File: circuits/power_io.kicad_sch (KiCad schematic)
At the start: 53 parts, among them J5 24V DC IN, J6 24V RJ45 IN, U11 AP2112K-3.3, U12 INA4180A1, U13 LM4040C50 5V, U14 AD7606BSTZ-4, U15 AP63205WU-7 5V BUCK, U16 AP63200WU-7 10.7V BUCK

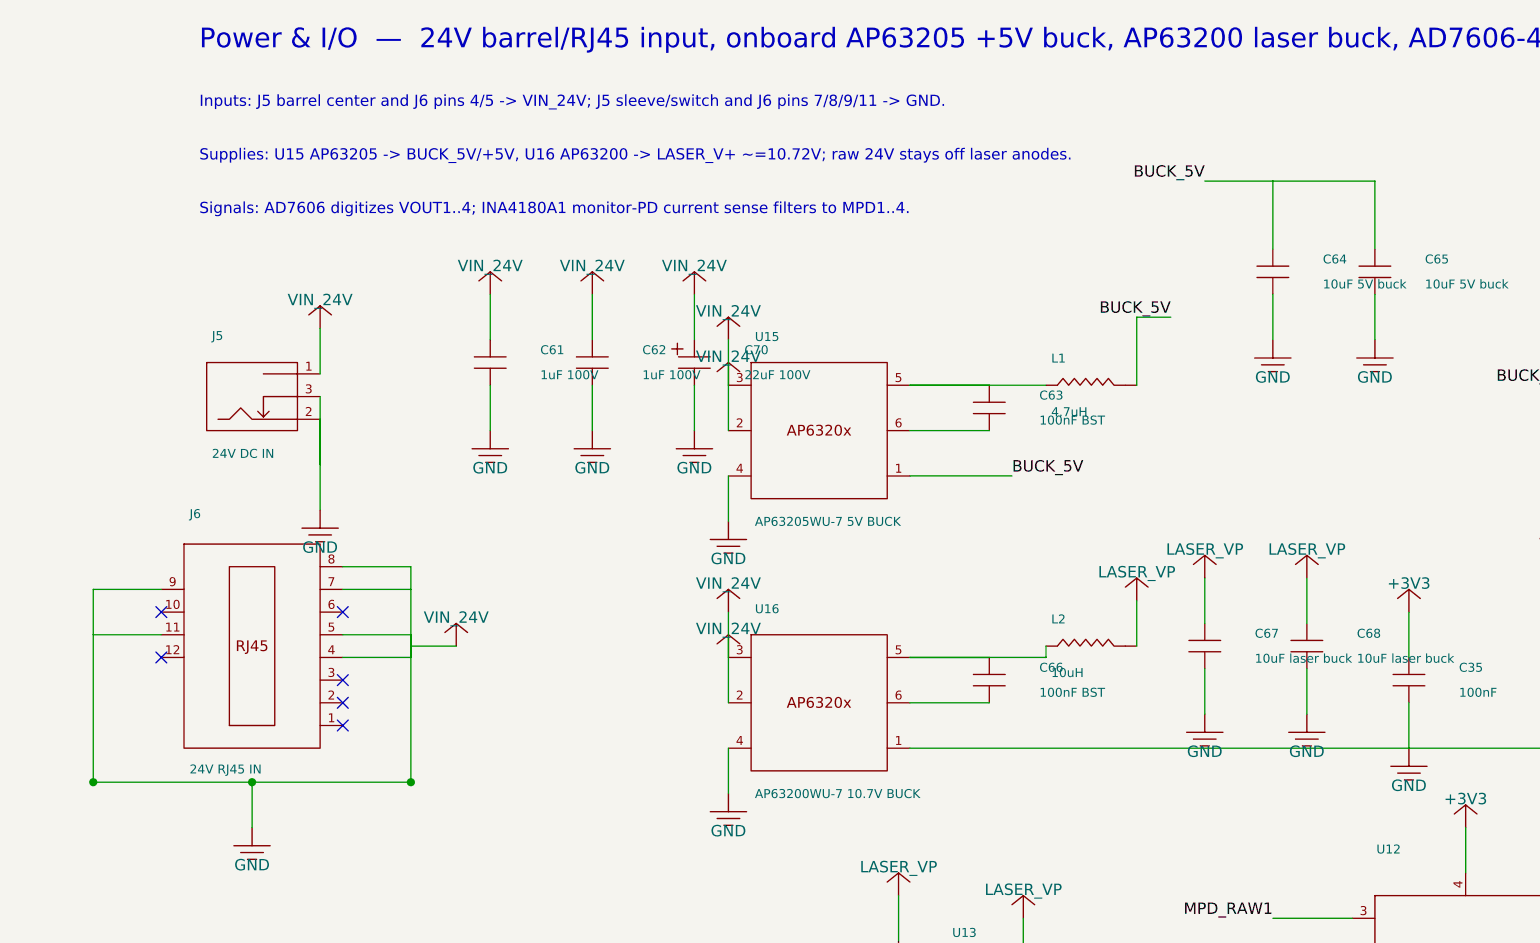
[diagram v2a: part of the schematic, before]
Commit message: Use access-controller RJ45 in power IO
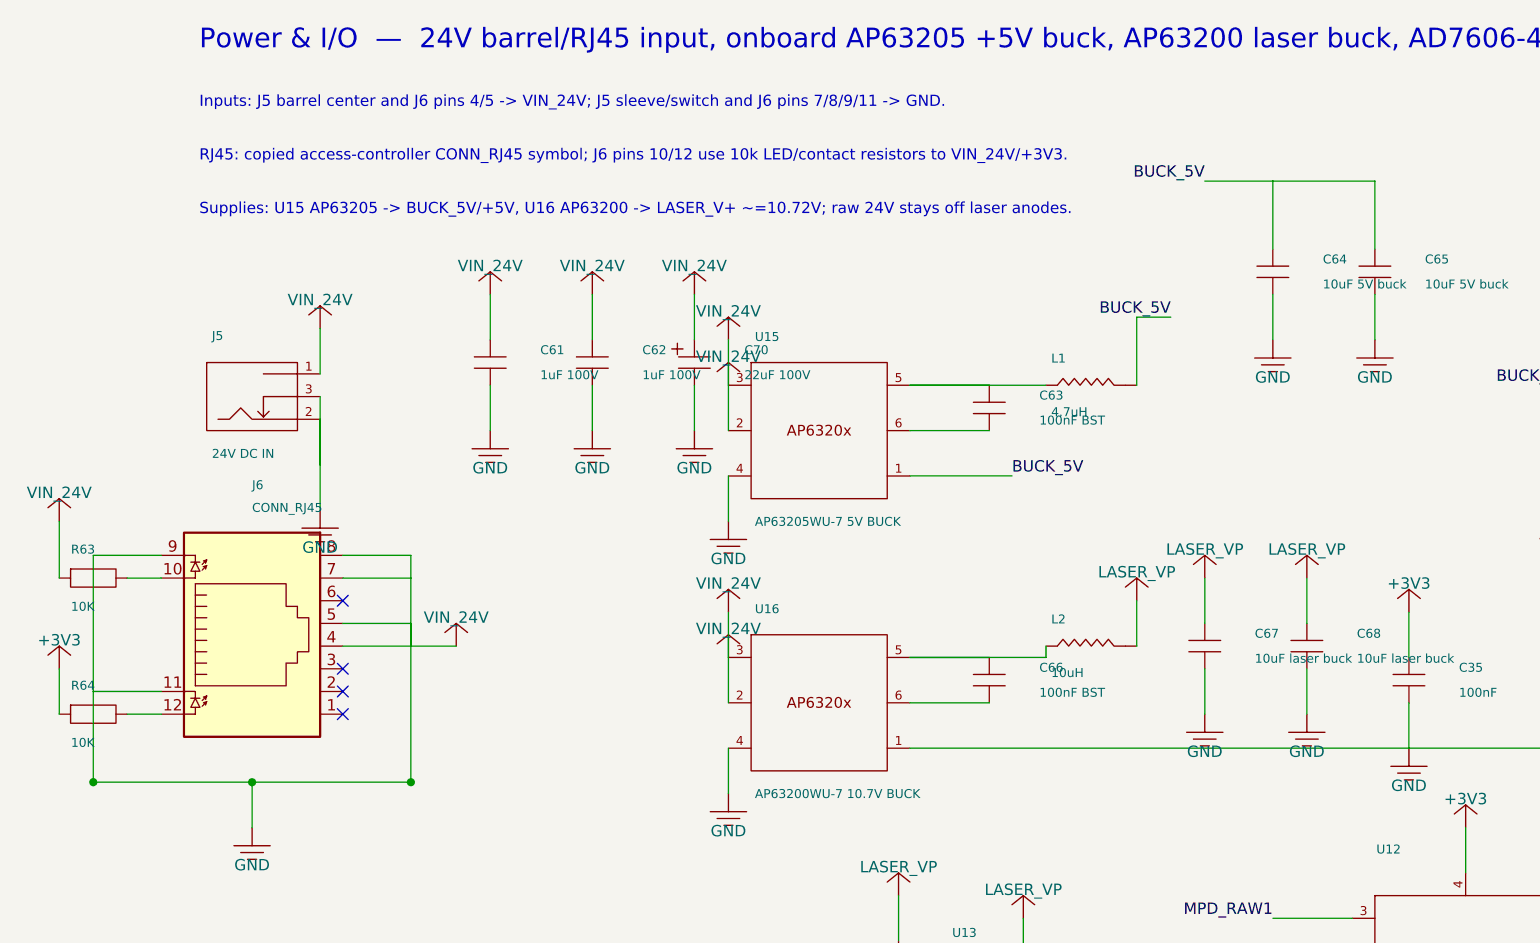
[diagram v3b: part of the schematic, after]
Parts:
- removed C35, C49: 100nF, Capacitor_SMD:C_0402_1005Metric_Pad0.74x0.62mm_HandSolder, symbol viv:C_V
- removed C36: 100nF MPD bias, Capacitor_SMD:C_0402_1005Metric_Pad0.74x0.62mm_HandSolder, symbol viv:C_V
- removed C51, C52: 100nF ADC AVCC, Capacitor_SMD:C_0402_1005Metric_Pad0.74x0.62mm_HandSolder, symbol viv:C_V
- removed C63, C66: 100nF BST, Capacitor_SMD:C_0402_1005Metric_Pad0.74x0.62mm_HandSolder, symbol viv:C_V
- removed L1: 4.7uH, Open_Automation:L_5.4x5.3_H3, symbol viv:L_H
- removed L2: 10uH, Open_Automation:L_4x4, symbol viv:L_H
- added C34: 10uF +5V bulk, Capacitor_SMD:C_0805_2012Metric_Pad1.18x1.45mm_HandSolder, symbol viv:C_V
- added C40: 100nF MPD ADC, Capacitor_SMD:C_0402_1005Metric_Pad0.74x0.62mm_HandSolder, symbol viv:C_V
- added C50: 10uF, Capacitor_SMD:C_0805_2012Metric_Pad1.18x1.45mm_HandSolder, symbol viv:C_V
- added C60: 10uF ADC REFCAP, Capacitor_SMD:C_0805_2012Metric_Pad1.18x1.45mm_HandSolder, symbol viv:C_V
- added C69: 100pF FF, Capacitor_SMD:C_0402_1005Metric_Pad0.74x0.62mm_HandSolder, symbol viv:C_V
- added C70: 22uF 100V, Capacitor_SMD:C_Elec_8x10.2, symbol viv:C_POL_V
- added R49: 1k ADC, Resistor_SMD:R_0603_1608Metric_Pad0.98x0.95mm_HandSolder, symbol viv:R_H
- added U12: INA4180A1, Package_SO:TSSOP-14_4.4x5mm_P0.65mm, symbol viv:INA4180_TSSOP14
- added U14: AD7606BSTZ-4, Package_QFP:LQFP-64_10x10mm_P0.5mm, symbol viv:AD7606_4
- added U15: AP63205WU-7 5V BUCK, Package_TO_SOT_SMD:TSOT-23-6, symbol viv:AP6320X_TSOT6
- added U16: AP63200WU-7 10.7V BUCK, Package_TO_SOT_SMD:TSOT-23-6, symbol viv:AP6320X_TSOT6
- C35: renamed from R41; value 2.49k MPD bias -> 100nF; footprint Resistor_SMD:R_0603_1608Metric_Pad0.98x0.95mm_HandSolder -> Capacitor_SMD:C_0402_1005Metric_Pad0.74x0.62mm_HandSolder; symbol viv:R_V -> viv:C_V; LCSC C2099849 -> C83056; Part Number CRCW06032K49FKEAHP -> 0402B104K160CT
- C36: renamed from R42; value 750R MPD sense -> 100nF MPD bias; footprint Resistor_SMD:R_0603_1608Metric_Pad0.98x0.95mm_HandSolder -> Capacitor_SMD:C_0402_1005Metric_Pad0.74x0.62mm_HandSolder; symbol viv:R_H -> viv:C_V; LCSC C114635 -> C83056; Part Number RC0603FR-07750RL -> 0402B104K160CT
- C37: renamed from R45; value 1k ADC -> 100nF MPD ADC; footprint Resistor_SMD:R_0603_1608Metric_Pad0.98x0.95mm_HandSolder -> Capacitor_SMD:C_0402_1005Metric_Pad0.74x0.62mm_HandSolder; symbol viv:R_H -> viv:C_V; LCSC C2907002 -> C83056; Part Number FRC0603F1001TS -> 0402B104K160CT
- C38: renamed from R47; value 1k ADC -> 100nF MPD ADC; footprint Resistor_SMD:R_0603_1608Metric_Pad0.98x0.95mm_HandSolder -> Capacitor_SMD:C_0402_1005Metric_Pad0.74x0.62mm_HandSolder; symbol viv:R_H -> viv:C_V; LCSC C2907002 -> C83056; Part Number FRC0603F1001TS -> 0402B104K160CT
- C39: renamed from R49; value 1k ADC -> 100nF MPD ADC; footprint Resistor_SMD:R_0603_1608Metric_Pad0.98x0.95mm_HandSolder -> Capacitor_SMD:C_0402_1005Metric_Pad0.74x0.62mm_HandSolder; symbol viv:R_H -> viv:C_V; LCSC C2907002 -> C83056; Part Number FRC0603F1001TS -> 0402B104K160CT
- C48: renamed from C50; value 10uF -> 1uF; footprint Capacitor_SMD:C_0805_2012Metric_Pad1.18x1.45mm_HandSolder -> Capacitor_SMD:C_0402_1005Metric_Pad0.74x0.62mm_HandSolder; LCSC C318691 -> C7472946; Part Number CL21A106KAYNNNG -> HGC0402R5105K250NTEJ
- C49: renamed from U16; value AP63200WU-7 10.7V BUCK -> 100nF; footprint Package_TO_SOT_SMD:TSOT-23-6 -> Capacitor_SMD:C_0402_1005Metric_Pad0.74x0.62mm_HandSolder; symbol viv:AP6320X_TSOT6 -> viv:C_V; LCSC C2071868 -> C83056; Part Number AP63200WU-7 -> 0402B104K160CT
- C53: renamed from C55; value 100nF ADC VDRIVE -> 100nF ADC AVCC
- C54: renamed from C56; value 10uF ADC AVCC -> 100nF ADC AVCC; footprint Capacitor_SMD:C_0805_2012Metric_Pad1.18x1.45mm_HandSolder -> Capacitor_SMD:C_0402_1005Metric_Pad0.74x0.62mm_HandSolder; LCSC C318691 -> C83056; Part Number CL21A106KAYNNNG -> 0402B104K160CT
- C55: renamed from C57; value 1uF ADC REGCAP -> 100nF ADC VDRIVE; LCSC C7472946 -> C83056; Part Number HGC0402R5105K250NTEJ -> 0402B104K160CT
- C56: renamed from C58; value 1uF ADC REGCAP -> 10uF ADC AVCC; footprint Capacitor_SMD:C_0402_1005Metric_Pad0.74x0.62mm_HandSolder -> Capacitor_SMD:C_0805_2012Metric_Pad1.18x1.45mm_HandSolder; LCSC C7472946 -> C318691; Part Number HGC0402R5105K250NTEJ -> CL21A106KAYNNNG
- C57: renamed from C59; value 10uF ADC REF -> 1uF ADC REGCAP; footprint Capacitor_SMD:C_0805_2012Metric_Pad1.18x1.45mm_HandSolder -> Capacitor_SMD:C_0402_1005Metric_Pad0.74x0.62mm_HandSolder; LCSC C318691 -> C7472946; Part Number CL21A106KAYNNNG -> HGC0402R5105K250NTEJ
- C58: renamed from C60; value 10uF ADC REFCAP -> 1uF ADC REGCAP; footprint Capacitor_SMD:C_0805_2012Metric_Pad1.18x1.45mm_HandSolder -> Capacitor_SMD:C_0402_1005Metric_Pad0.74x0.62mm_HandSolder; LCSC C318691 -> C7472946; Part Number CL21A106KAYNNNG -> HGC0402R5105K250NTEJ
- C59: renamed from U12; value INA4180A1 -> 10uF ADC REF; footprint Package_SO:TSSOP-14_4.4x5mm_P0.65mm -> Capacitor_SMD:C_0805_2012Metric_Pad1.18x1.45mm_HandSolder; symbol viv:INA4180_TSSOP14 -> viv:C_V; LCSC C2057528 -> C318691; Part Number INA4180A1IPWR -> CL21A106KAYNNNG
- C61: renamed from C70; value 22uF 100V -> 1uF 100V; footprint Capacitor_SMD:C_Elec_8x10.2 -> Capacitor_SMD:C_1206_3216Metric_Pad1.33x1.80mm_HandSolder; symbol viv:C_POL_V -> viv:C_V; LCSC C90264 -> C13832; Part Number RVT2A220M0810 -> CL31B105KCHNNNE
- C62: renamed from U15; value AP63205WU-7 5V BUCK -> 1uF 100V; footprint Package_TO_SOT_SMD:TSOT-23-6 -> Capacitor_SMD:C_1206_3216Metric_Pad1.33x1.80mm_HandSolder; symbol viv:AP6320X_TSOT6 -> viv:C_V; LCSC C2071056 -> C13832; Part Number AP63205WU-7 -> CL31B105KCHNNNE
- C63: renamed from C65; value 10uF 5V buck -> 100nF BST; footprint Capacitor_SMD:C_0805_2012Metric_Pad1.18x1.45mm_HandSolder -> Capacitor_SMD:C_0402_1005Metric_Pad0.74x0.62mm_HandSolder; LCSC C318691 -> C83056; Part Number CL21A106KAYNNNG -> 0402B104K160CT
- C64: renamed from D5; value SS14 -> 10uF 5V buck; footprint Diode_SMD:D_SMA -> Capacitor_SMD:C_0805_2012Metric_Pad1.18x1.45mm_HandSolder; symbol viv:SCHOTTKY -> viv:C_V; LCSC C2480 -> C318691; Part Number SS14 -> CL21A106KAYNNNG
- C65: renamed from D6; value SS14 -> 10uF 5V buck; footprint Diode_SMD:D_SMA -> Capacitor_SMD:C_0805_2012Metric_Pad1.18x1.45mm_HandSolder; symbol viv:SCHOTTKY -> viv:C_V; LCSC C2480 -> C318691; Part Number SS14 -> CL21A106KAYNNNG
- C66: renamed from C68; value 10uF laser buck -> 100nF BST; footprint Capacitor_SMD:C_0805_2012Metric_Pad1.18x1.45mm_HandSolder -> Capacitor_SMD:C_0402_1005Metric_Pad0.74x0.62mm_HandSolder; LCSC C318691 -> C83056; Part Number CL21A106KAYNNNG -> 0402B104K160CT
- C67: renamed from R61; value 274k FB -> 10uF laser buck; footprint Resistor_SMD:R_0603_1608Metric_Pad0.98x0.95mm_HandSolder -> Capacitor_SMD:C_0805_2012Metric_Pad1.18x1.45mm_HandSolder; symbol viv:R_V -> viv:C_V; LCSC C2942027 -> C318691; Part Number FRC0603F2743TS -> CL21A106KAYNNNG
- C68: renamed from R62; value 22.1K FB -> 10uF laser buck; footprint Resistor_SMD:R_0402_1005Metric_Pad0.72x0.64mm_HandSolder -> Capacitor_SMD:C_0805_2012Metric_Pad1.18x1.45mm_HandSolder; symbol viv:R_V -> viv:C_V; LCSC C2929993 -> C318691; Part Number FRC0402F2212TS -> CL21A106KAYNNNG
- D5: renamed from C34; value 10uF +5V bulk -> SS14; footprint Capacitor_SMD:C_0805_2012Metric_Pad1.18x1.45mm_HandSolder -> Diode_SMD:D_SMA; symbol viv:C_V -> viv:SCHOTTKY; LCSC C318691 -> C2480; Part Number CL21A106KAYNNNG -> SS14
- D6: renamed from U11; value AP2112K-3.3 -> SS14; footprint Package_TO_SOT_SMD:SOT-23-5 -> Diode_SMD:D_SMA; symbol viv:LDO5 -> viv:SCHOTTKY; LCSC C51118 -> C2480; Part Number AP2112K-3.3TRG1 -> SS14
- J6: value 24V RJ45 IN -> CONN_RJ45; symbol viv:CONN_RJ45 -> open_automation:CONN_RJ45
- L1: renamed from C64; value 10uF 5V buck -> 4.7uH; footprint Capacitor_SMD:C_0805_2012Metric_Pad1.18x1.45mm_HandSolder -> Open_Automation:L_5.4x5.3_H3; symbol viv:C_V -> viv:L_H; LCSC C318691 -> C408410; Part Number CL21A106KAYNNNG -> MWSA0503S-4R7MT
- L2: renamed from C67; value 10uF laser buck -> 10uH; footprint Capacitor_SMD:C_0805_2012Metric_Pad1.18x1.45mm_HandSolder -> Open_Automation:L_4x4; symbol viv:C_V -> viv:L_H; LCSC C318691 -> C98364; Part Number CL21A106KAYNNNG -> WPN4020H100MT
- R41: renamed from R43; value 1k ADC -> 2.49k MPD bias; symbol viv:R_H -> viv:R_V; LCSC C2907002 -> C2099849; Part Number FRC0603F1001TS -> CRCW06032K49FKEAHP
- R42: renamed from C37; value 100nF MPD ADC -> 750R MPD sense; footprint Capacitor_SMD:C_0402_1005Metric_Pad0.74x0.62mm_HandSolder -> Resistor_SMD:R_0603_1608Metric_Pad0.98x0.95mm_HandSolder; symbol viv:C_V -> viv:R_H; LCSC C83056 -> C114635; Part Number 0402B104K160CT -> RC0603FR-07750RL
- R43: renamed from R44; value 750R MPD sense -> 1k ADC; LCSC C114635 -> C2907002; Part Number RC0603FR-07750RL -> FRC0603F1001TS
- R44: renamed from C38; value 100nF MPD ADC -> 750R MPD sense; footprint Capacitor_SMD:C_0402_1005Metric_Pad0.74x0.62mm_HandSolder -> Resistor_SMD:R_0603_1608Metric_Pad0.98x0.95mm_HandSolder; symbol viv:C_V -> viv:R_H; LCSC C83056 -> C114635; Part Number 0402B104K160CT -> RC0603FR-07750RL
- R45: renamed from R46; value 750R MPD sense -> 1k ADC; LCSC C114635 -> C2907002; Part Number RC0603FR-07750RL -> FRC0603F1001TS
- R46: renamed from C39; value 100nF MPD ADC -> 750R MPD sense; footprint Capacitor_SMD:C_0402_1005Metric_Pad0.74x0.62mm_HandSolder -> Resistor_SMD:R_0603_1608Metric_Pad0.98x0.95mm_HandSolder; symbol viv:C_V -> viv:R_H; LCSC C83056 -> C114635; Part Number 0402B104K160CT -> RC0603FR-07750RL
- R47: renamed from R48; value 750R MPD sense -> 1k ADC; LCSC C114635 -> C2907002; Part Number RC0603FR-07750RL -> FRC0603F1001TS
- R48: renamed from C40; value 100nF MPD ADC -> 750R MPD sense; footprint Capacitor_SMD:C_0402_1005Metric_Pad0.74x0.62mm_HandSolder -> Resistor_SMD:R_0603_1608Metric_Pad0.98x0.95mm_HandSolder; symbol viv:C_V -> viv:R_H; LCSC C83056 -> C114635; Part Number 0402B104K160CT -> RC0603FR-07750RL
- R61: renamed from C69; value 100pF FF -> 274k FB; footprint Capacitor_SMD:C_0402_1005Metric_Pad0.74x0.62mm_HandSolder -> Resistor_SMD:R_0603_1608Metric_Pad0.98x0.95mm_HandSolder; symbol viv:C_V -> viv:R_V; LCSC C1546 -> C2942027; Part Number 0402CG101J500NT -> FRC0603F2743TS
- R62: renamed from U14; value AD7606BSTZ-4 -> 22.1K FB; footprint Package_QFP:LQFP-64_10x10mm_P0.5mm -> Resistor_SMD:R_0402_1005Metric_Pad0.72x0.64mm_HandSolder; symbol viv:AD7606_4 -> viv:R_V; LCSC C51512 -> C2929993; Part Number AD7606BSTZ-4RL -> FRC0402F2212TS
- R63: renamed from C61; value 1uF 100V -> 10K; footprint Capacitor_SMD:C_1206_3216Metric_Pad1.33x1.80mm_HandSolder -> Resistor_SMD:R_0603_1608Metric_Pad0.98x0.95mm_HandSolder; symbol viv:C_V -> viv:R_H_RJ45; LCSC C13832 -> C844918; Part Number CL31B105KCHNNNE -> CRCW060310K0FKEA
- R64: renamed from C62; value 1uF 100V -> 10K; footprint Capacitor_SMD:C_1206_3216Metric_Pad1.33x1.80mm_HandSolder -> Resistor_SMD:R_0603_1608Metric_Pad0.98x0.95mm_HandSolder; symbol viv:C_V -> viv:R_H_RJ45; LCSC C13832 -> C844918; Part Number CL31B105KCHNNNE -> CRCW060310K0FKEA
- U11: renamed from C48; value 1uF -> AP2112K-3.3; footprint Capacitor_SMD:C_0402_1005Metric_Pad0.74x0.62mm_HandSolder -> Package_TO_SOT_SMD:SOT-23-5; symbol viv:C_V -> viv:LDO5; LCSC C7472946 -> C51118; Part Number HGC0402R5105K250NTEJ -> AP2112K-3.3TRG1
- renumbered C53 to C51, C54 to C52
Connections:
- net +3V3: now also C35.1, C49.1, C55.1, R64.1, U11.5 (VOUT), C50.1, U12.4 (VS), U14.23 (VDRIVE), U14.34 (REF SELECT), U14.6 (PAR/SER/BYTE SEL), U14.7 (STBY); no longer C48.1, C53.1, C59.4 (VS), D6.5 (VOUT), R62.23 (VDRIVE), R62.34 (REF SELECT), R62.6 (PAR/SER/BYTE SEL), R62.7 (STBY)
- net +5V: now also C48.1, C53.1, C56.1, D5.2 (K), D6.2 (K), U11.3 (EN), C34.1, U14.1 (AVCC), U14.37 (AVCC), U14.38 (AVCC), U14.48 (AVCC); no longer C64.2 (K), C65.2 (K), D5.1, D6.1 (VIN), D6.3 (EN), R62.1 (AVCC), R62.37 (AVCC), R62.38 (AVCC), R62.48 (AVCC)
- net ADC_BUSY: now also U14.14 (BUSY); no longer R62.14 (BUSY)
- net ADC_CS: now also U14.13 (CS); no longer R62.13 (CS)
- net ADC_MISO_A: now also U14.24 (DB7/DOUTA); no longer R62.24 (DB7/DOUTA)
- net ADC_MISO_B: now also U14.25 (DB8/DOUTB); no longer R62.25 (DB8/DOUTB)
- net ADC_RESET: now also U14.11 (RESET); no longer R62.11 (RESET)
- net ADC_SCLK: now also U14.12 (RD/SCLK); no longer R62.12 (RD/SCLK)
- net BUCK_5V: now also C64.1, D6.1 (A), L1.2, U15.1 (FB); no longer C62.1 (FB), C63.1, L1.1
- net CONVST: now also U14.10 (CONVSTB), U14.9 (CONVSTA); no longer R62.10 (CONVSTB), R62.9 (CONVSTA)
- net GND: now also C37.2, C38.2, C39.2, C59.2, C62.1, C64.2, C65.2, C67.2, R41.2, C34.2, C40.2, C50.2, C60.2, C70.1 (+), C70.2 (-), U12.11 (GND), U14.16 (DB0), U14.17 (DB1), U14.18 (DB2), U14.19 (DB3), U14.2 (AGND), U14.20 (DB4), U14.21 (DB5), U14.22 (DB6), U14.26 (AGND), U14.27 (DB9), U14.28 (DB10), U14.29 (DB11), U14.3 (OS0), U14.30 (DB12), U14.31 (DB13), U14.32 (DB14/HBEN), U14.33 (DB15/BYTE SEL), U14.35 (AGND), U14.4 (OS1), U14.40 (AGND), U14.41 (AGND), U14.43 (REFGND), U14.46 (REFGND), U14.47 (AGND), U14.5 (OS2), U14.50 (V1GND), U14.52 (V2GND), U14.53 (AGND), U14.54 (AGND), U14.55 (AGND), U14.56 (AGND), U14.58 (V3GND), U14.60 (V4GND), U14.61 (AGND), U14.62 (AGND), U14.63 (AGND), U14.64 (AGND), U14.8 (RANGE), U15.2 (EN), U15.3 (IN), U15.4 (GND), U16.2 (EN), U16.3 (IN), U16.4 (GND); no longer C49.3 (IN), C49.4 (GND), C59.11 (GND), C62.3 (IN), C62.4 (GND), C63.2, C66.2, D5.2, D6.2 (GND), L1.2, L2.2, R42.2, R44.2, R46.2, R48.2, R62.16 (DB0), R62.17 (DB1), R62.18 (DB2), R62.19 (DB3), R62.20 (DB4), R62.21 (DB5), R62.22 (DB6), R62.26 (AGND), R62.27 (DB9), R62.28 (DB10), R62.29 (DB11), R62.3 (OS0), R62.30 (DB12), R62.31 (DB13), R62.32 (DB14/HBEN), R62.33 (DB15/BYTE SEL), R62.35 (AGND), R62.4 (OS1), R62.40 (AGND), R62.41 (AGND), R62.43 (REFGND), R62.46 (REFGND), R62.47 (AGND), R62.5 (OS2), R62.50 (V1GND), R62.52 (V2GND), R62.53 (AGND), R62.54 (AGND), R62.55 (AGND), R62.56 (AGND), R62.58 (V3GND), R62.60 (V4GND), R62.61 (AGND), R62.62 (AGND), R62.63 (AGND), R62.64 (AGND), R62.8 (RANGE), R63.2, R64.1, R64.2
- net LASER_V+: now also C36.1, C68.1, L2.2, C69.1; no longer C66.1, L2.1
- net MPD1: now also C37.1, R43.2; no longer R41.2, R42.1
- net MPD2: now also C38.1, R45.2; no longer C37.2, R44.1
- net MPD3: now also C39.1, R47.2; no longer C38.2, R46.1
- net MPD4: now also C40.1, R49.2; no longer C39.2, R48.1
- net MPD_AMP1: now also R43.1, U12.1 (OUT1); no longer C59.1 (OUT1), R41.1
- net MPD_AMP2: now also R45.1, U12.7 (OUT2); no longer C37.1, C59.7 (OUT2)
- net MPD_AMP3: now also R47.1, U12.8 (OUT3); no longer C38.1, C59.8 (OUT3)
- net MPD_AMP4: now also R49.1, U12.14 (OUT4); no longer C39.1, C59.14 (OUT4)
- net MPD_BIAS: now also R41.1, R42.2, R44.2, R46.2, R48.2, U12.13 (IN-4), U12.2 (IN-1), U12.6 (IN-2), U12.9 (IN-3); no longer C35.1, C59.13 (IN-4), C59.2 (IN-1), C59.6 (IN-2), C59.9 (IN-3), R43.2, R45.2, R47.2
- net MPD_RAW1: now also R42.1, U12.3 (IN+1); no longer C36.1, C59.3 (IN+1)
- net MPD_RAW2: now also R44.1, U12.5 (IN+2); no longer C59.5 (IN+2), R43.1
- net MPD_RAW3: now also R46.1, U12.10 (IN+3); no longer C59.10 (IN+3), R45.1
- net MPD_RAW4: now also R48.1, U12.12 (IN+4); no longer C59.12 (IN+4), R47.1
- net VBUS_5V: now also D5.1 (A); no longer C64.1 (A)
- net VOUT1: now also U14.49 (V1); no longer R62.49 (V1)
- net VOUT2: now also U14.51 (V2); no longer R62.51 (V2)
- net VOUT3: now also U14.57 (V3); no longer R62.57 (V3)
- net VOUT4: now also U14.59 (V4); no longer R62.59 (V4)
- net at J6.10: now also R63.2
- net at J6.12: now also R64.2
- net at C57.1: now also U14.36 (REGCAP); no longer R62.42 (REFIN/REFOUT)
- new net: C63.1, L1.1, U15.5 (SW)
- new net: C63.2, U15.6 (BST)
- new net: C69.2, R61.2, R62.1, U16.1 (FB)
- new net: C66.1, L2.1, U16.5 (SW)
- new net: C66.2, U16.6 (BST)
- new net: C58.1, U14.39 (REGCAP)
- new net: C59.1, U14.42 (REFIN/REFOUT)
- new net: C60.1, U14.44 (REFCAPA), U14.45 (REFCAPB)
- no-connect marks 8 -> 6
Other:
- note added: "RJ45: copied access-controller CONN_RJ45 symbol; J6 pins 10/12 use 10k LED/contact resistors to VIN_24V/+3V3."
- note removed: "Signals: AD7606 digitizes VOUT1..4; INA4180A1 monitor-PD current sense filters to MPD1..4."
- moved on the sheet: C48, C51, C52, C53, C54, C55, C56, C57, C58, C63, C66, R41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

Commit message: Spread out power IO schematic
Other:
- note added: "Power & I/O - 24V barrel/RJ45 input, onboard AP63205 +5V buck, AP63200 laser buck, AD7606-4 ADC, monitor-PD front end"
- note removed: "Power & I/O — 24V barrel/RJ45 input, onboard AP63205 +5V buck, AP63200 laser buck, AD7606-4 ADC, monitor-PD front end"
- moved on the sheet: C34, C35, C36, C37, C38, C39, C40, C48, C49, C50, C51, C52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
